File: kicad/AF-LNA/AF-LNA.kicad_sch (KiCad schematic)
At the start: 74 parts, among them J1 IN_SMA, J2 USB_C_Power_only, J3 LED Peak, J4 OUT_SMA, J5 LED PWR Good, Q1 2SC1815, Q2 2SC1815, SW1 SW_Short, U1 ADA4522-2, U2 ADA4522-2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

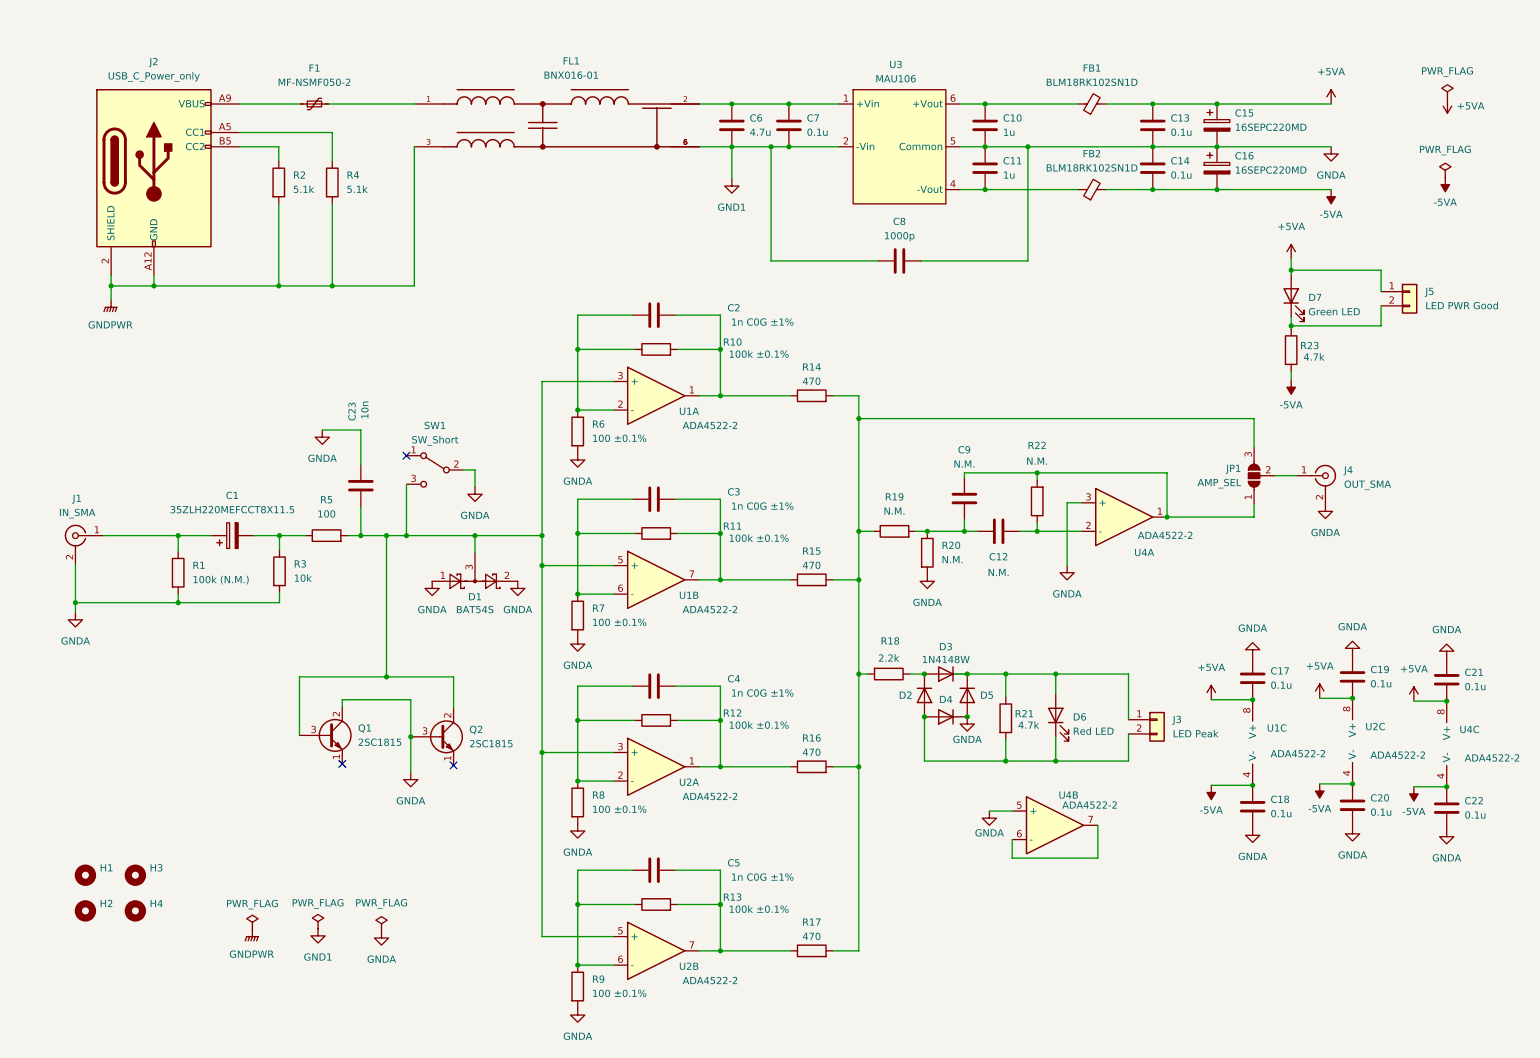
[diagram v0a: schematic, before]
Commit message: Update Rev1.1
SW1位置変更、帰還抵抗GND配線をIN側SMA端子から取るように変更
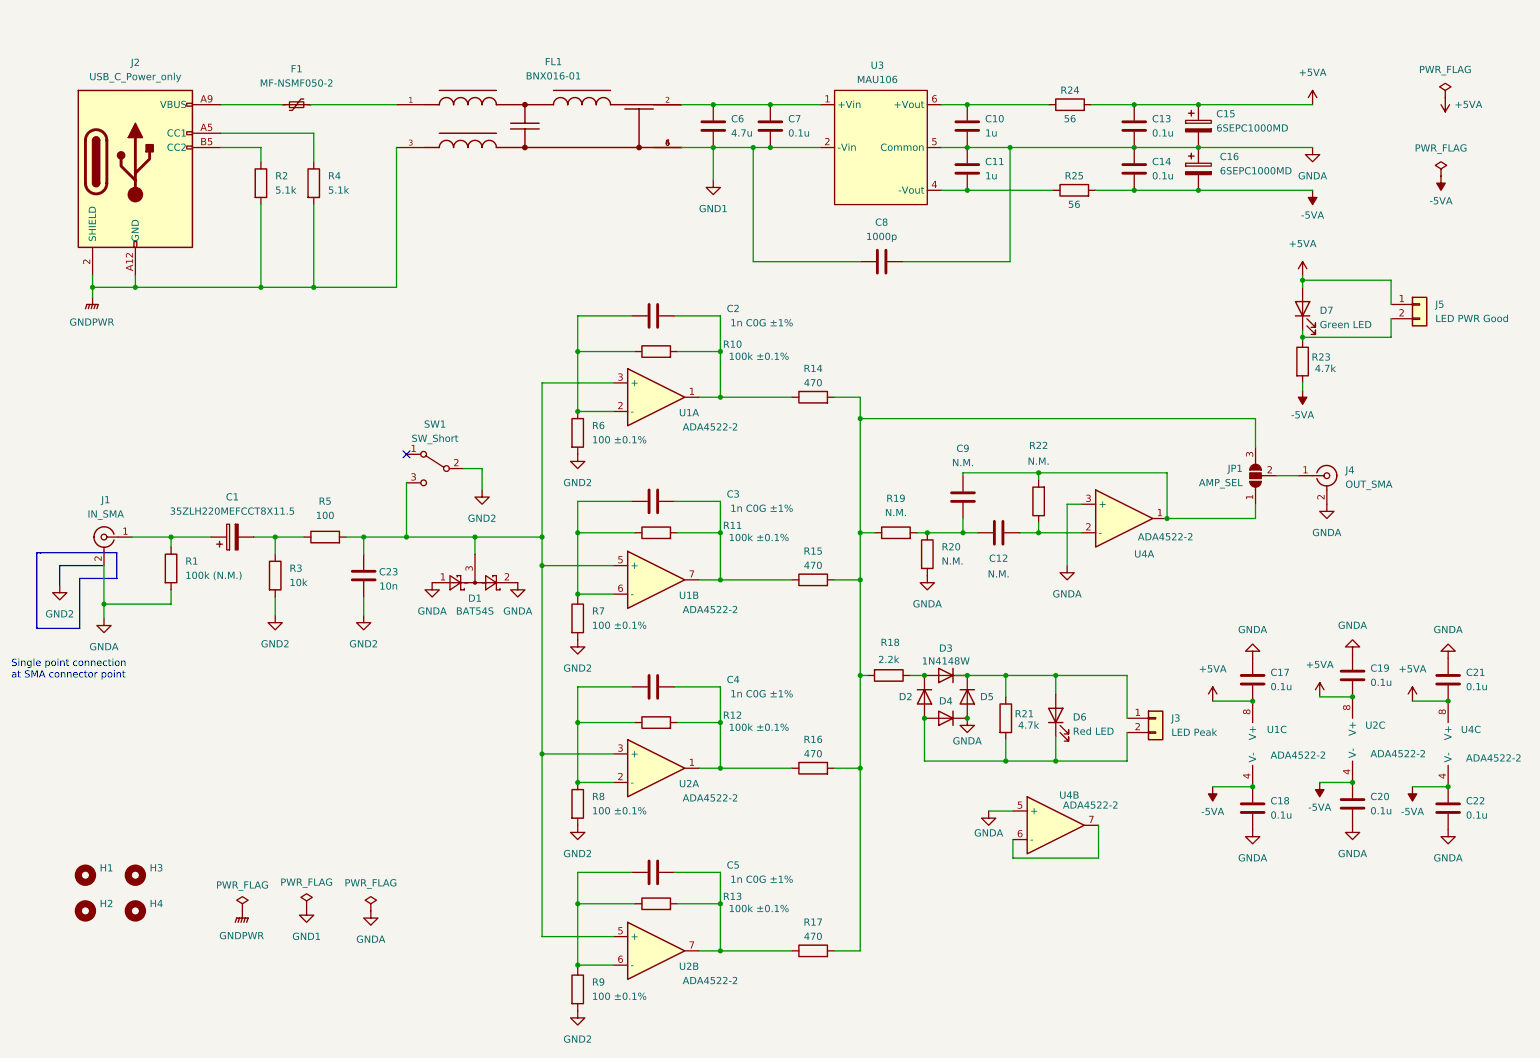
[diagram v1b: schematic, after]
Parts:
- removed FB1, FB2: BLM18RK102SN1D, Inductor_SMD:L_0603_1608Metric, symbol Device:FerriteBead_Small
- removed Q1, Q2: 2SC1815, Package_TO_SOT_THT:TO-92_Inline, symbol Transistor_BJT:2SC1815
- added R24, R25: 56, Resistor_SMD:R_0603_1608Metric, symbol Device:R
- C15, C16: value 16SEPC220MD -> 6SEPC1000MD
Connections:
- net +5VA: now also R24.2
- net -5VA: now also R25.2
- net GNDA: no longer C23.2, R3.2, R6.2, R7.2, R8.2, R9.2, SW1.2 (B)
- net at D1.3, R5.2, SW1.3 (C)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: now also C23.2; no longer C23.1
- net at C10.1, U3.6 (+Vout): now also R24.1
- net at C11.2, U3.4 (-Vout): now also R25.1
- new net GND2: C23.1, R3.2, R6.2, R7.2, R8.2, R9.2, SW1.2 (B)
- no-connect marks 3 -> 1
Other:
- note added: "Single point connection at SMA connector point"
- moved on the sheet: C10, C11, C13, C14, C15, C16, C23, C6, C7, C8, D7, F1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
